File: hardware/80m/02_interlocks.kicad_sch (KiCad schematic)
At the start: 15 parts, among them Q201 DMN2056U-7, U201 MCP100T-300I/TT, U202 74HC123D,653, U203 74HC14D,653

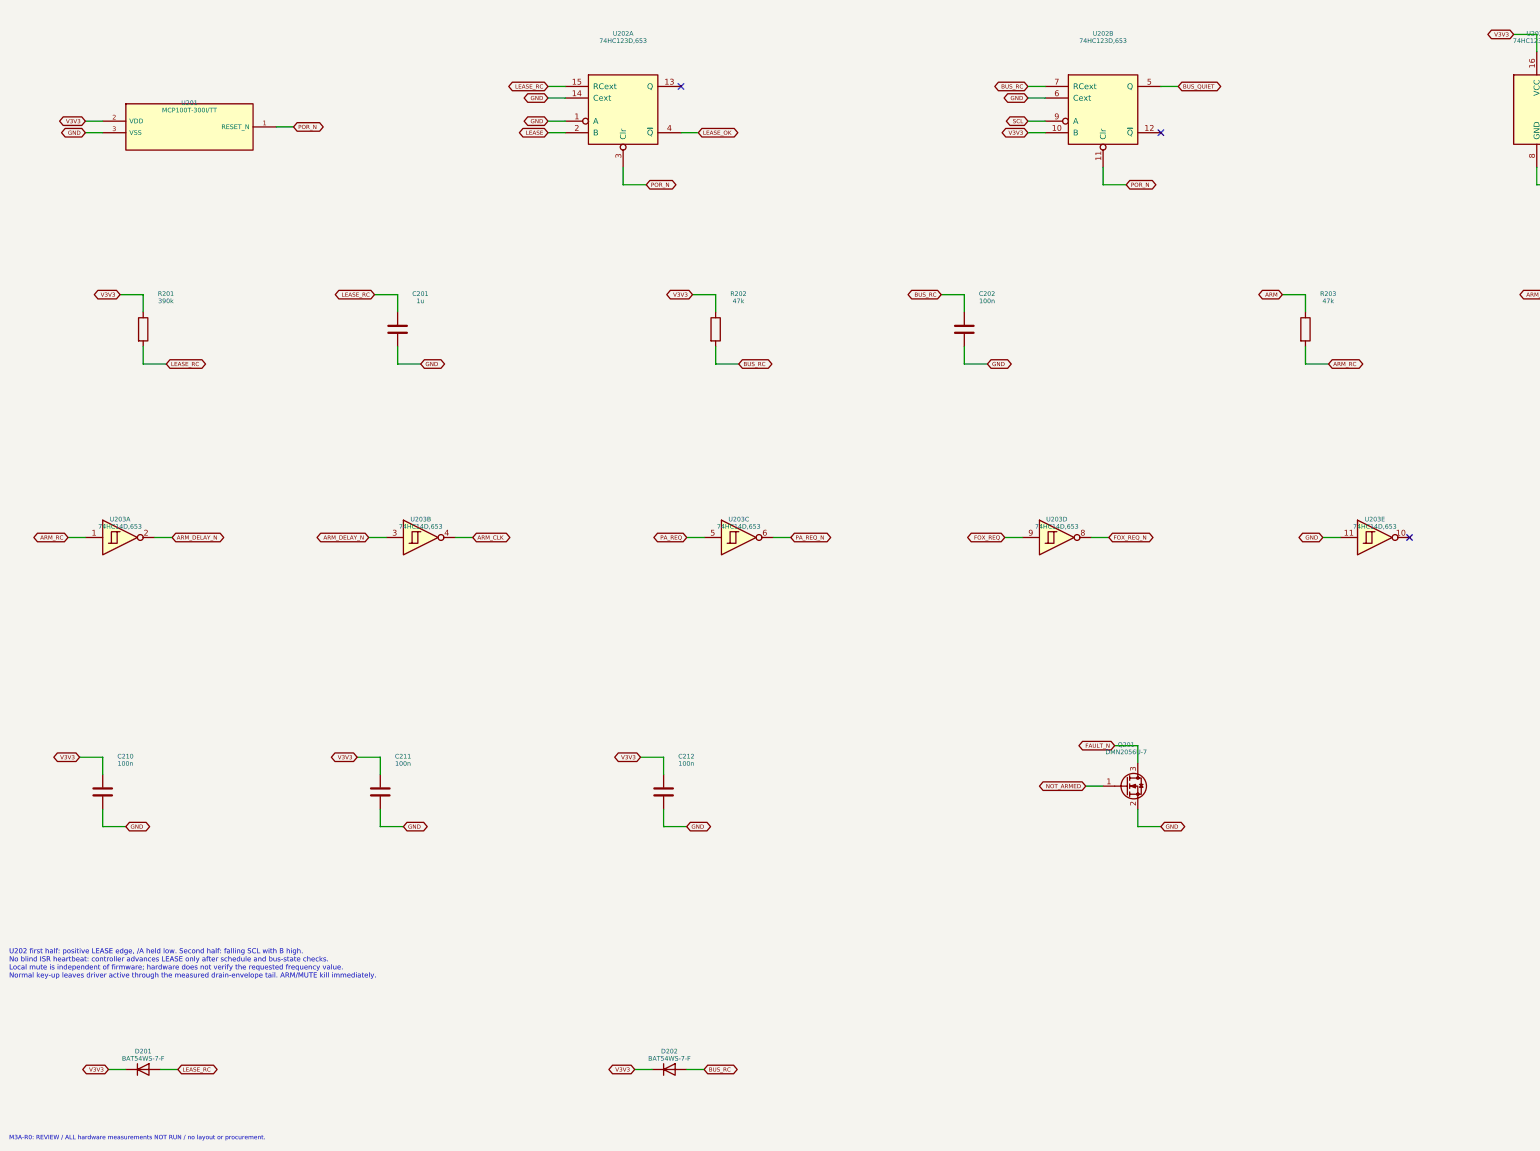
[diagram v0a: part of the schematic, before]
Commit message: Correct RF80 timer polarities and arming logic for M3A-R1 review
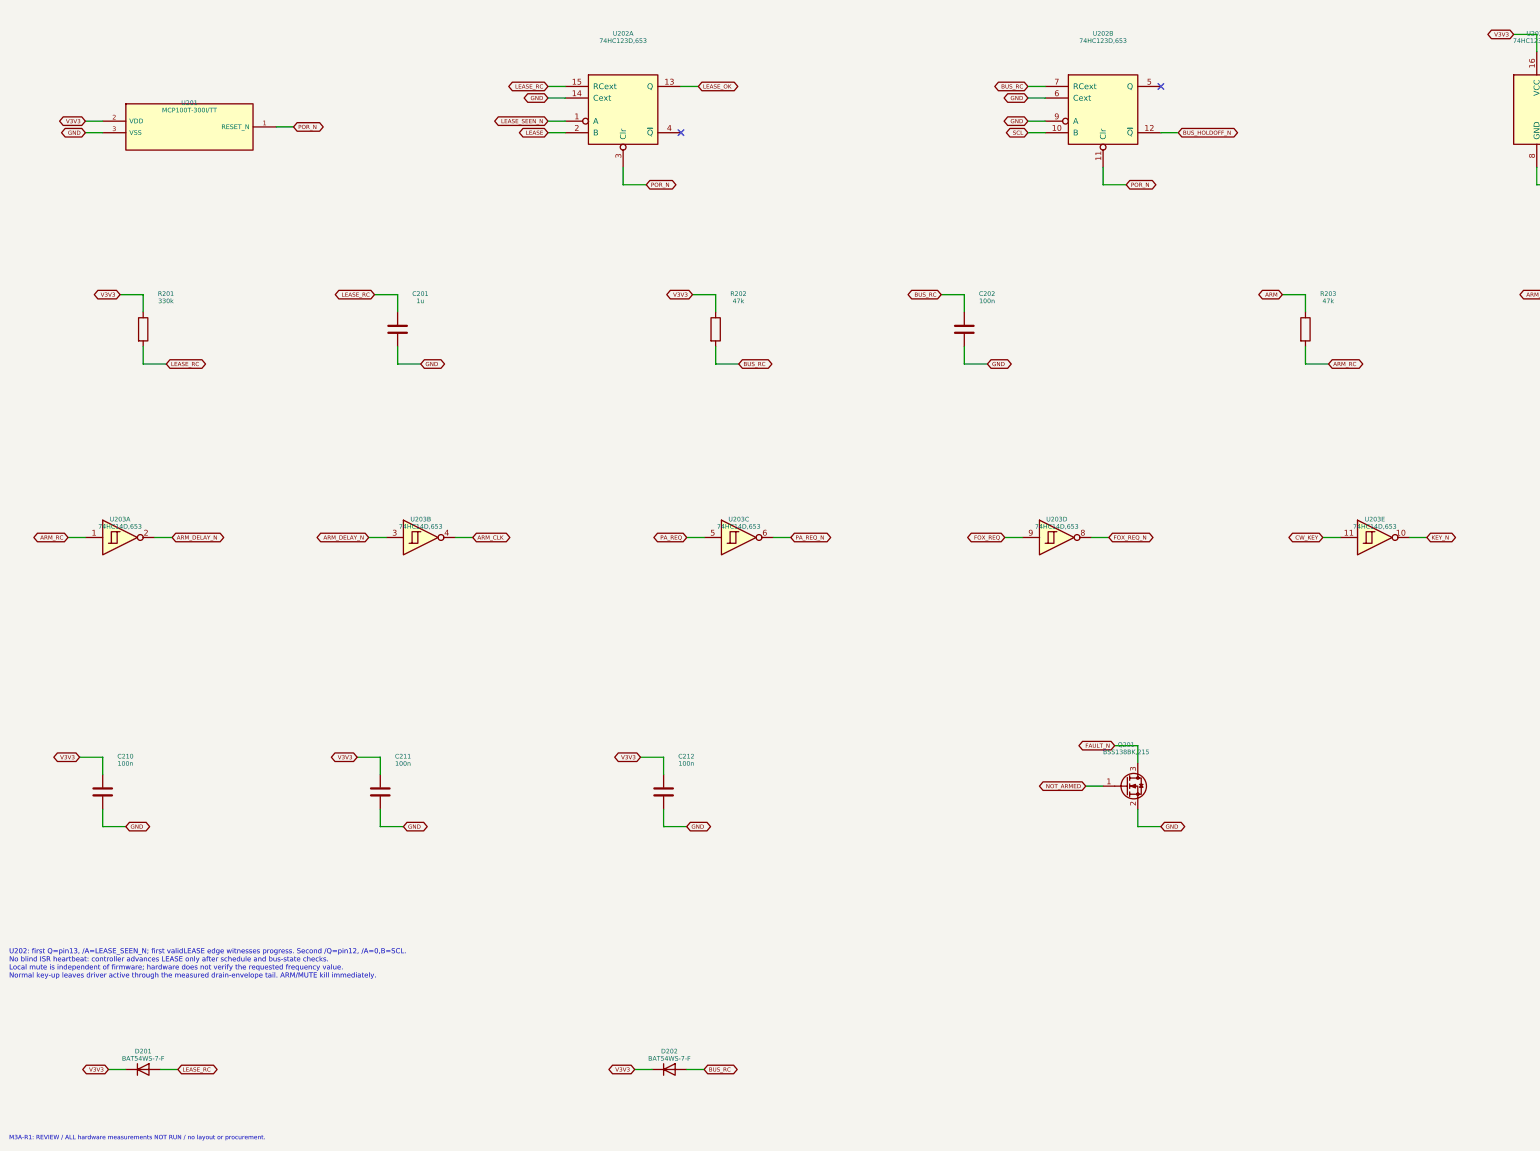
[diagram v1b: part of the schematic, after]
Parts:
- C201: Engineering_Note t=KRC approx0.176s at K0.45; characterize 3.3V,tolerance,te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 -> t=KRC approx0.165s at assumedK0.50; characterize 3.3V,toler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
- C202: Engineering_Note Approx2ms quiet delay; every falling SCL edge triggers; tes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 -> Approx2.35ms quiet delay at assumedK0.50; risingSCL and qua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
- Q201: value DMN2056U-7 -> BSS138BK,215; Engineering_Note Open-drain status; unarmed, not only faults. Pull on controller rail. 20VDS, +/-8VGS;45mohm at2.5V. Native2N7002 drawing only, actualMPN DMN2056U:1G2S3D; all switchednodes<9V. -> Open-drain status; unarmed, not only faults. Pull on controller rail. 60VDS,+/-20VGS;6.5ohm max at2.5V/10mA. Low-current function only; 1G2S3D. Ten-price observed; other prices estimates.; MPN DMN2056U-7 -> BSS138BK,215
- R201: value 390k -> 330k; MPN RC0603FR-07390KL -> RC0603FR-07330KL
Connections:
- net GND: now also U202.9 (A); no longer U202.1 (A), U203.11
- net LEASE_OK: now also U202.13 (Q); no longer U202.4 (~{Q})
- net SCL: now also U202.10 (B); no longer U202.9 (A)
- net V3V3: no longer U202.10 (B)
- net KEY_N: now reaches U203.10
- net BUS_HOLDOFF_N: now reaches U202.12 (~{Q})
- net BUS_QUIET: no longer names the net of U202.5 (Q)
- new net CW_KEY: U203.11
- new net LEASE_SEEN_N: U202.1 (A)
- no-connect marks 3 -> 2
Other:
- note added: "M3A-R1: REVIEW / ALL hardware measurements NOT RUN / no layout or procurement."
- note added: "U202: first Q=pin13, /A=LEASE_SEEN_N; first validLEASE edge witnesses progress. Second /Q=pin12, /A=0,B=SCL. No blind ISR heartbeat: controller advances LEASE only after schedule and bus-state checks. Local mute is independent of firmware; hardware does not verify the requested frequency value. Normal key-up leaves driver active through the measured drain-envelope tail. ARM/MUTE kill immediately."
- note removed: "M3A-R0: REVIEW / ALL hardware measurements NOT RUN / no layout or procurement."
- note removed: "U202 first half: positive LEASE edge, /A held low. Second half: falling SCL with B high. No blind ISR heartbeat: controller advances LEASE only after schedule and bus-state checks. Local mute is independent of firmware; hardware does not verify the requested frequency value. Normal key-up leaves driver active through the measured drain-envelope tail. ARM/MUTE kill immediately."

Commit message: Preserve M3B-E1 evaluation PCB before independent-review corrections
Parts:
- C202: Engineering_Note Approx2.35ms quiet delay at assumedK0.50; risingSCL and qualifiedRD-release trigger; test actual bound. Dated M2 distributor observation; no fresh basket verification. -> Approx2.35ms quiet delay at assumedK0.50; risingSCL and qualifiedRD-release trigger; test actual bound.
- C203, C210, C211, C212: Engineering_Note Dated M2 distributor observation; no fresh basket verificat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 -> (none)
- U201: Engineering_Note SOT23 pin1 RESET,2 VDD,3 VSS; nominal3.0V. Controller POR cannot replace unplugged-module local reset. Dated M2 distributor observation; no fresh basket verification. -> SOT23 pin1 RESET,2 VDD,3 VSS; nominal3.0V. Controller POR cannot replace unplugged-module local reset.
- U202: Engineering_Note CMOS 3.3 V. Supply unit and all unused gates explicitly connected. Dated M2 distributor observation; no fresh basket verification. -> CMOS 3.3 V. Supply unit and all unused gates explicitly connected.
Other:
- note added: "M3B-E1: REVIEW / ALL hardware measurements NOT RUN / no ordering or manufacture."
- note removed: "M3A-R1: REVIEW / ALL hardware measurements NOT RUN / no layout or procurement."

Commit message: Correct RF80 M3B-E2 physical pinouts and audit manufacturing readiness
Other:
- note added: "M3B-E2: REVIEW / ALL hardware measurements NOT RUN / no ordering or manufacture."
- note removed: "M3B-E1: REVIEW / ALL hardware measurements NOT RUN / no ordering or manufacture."
